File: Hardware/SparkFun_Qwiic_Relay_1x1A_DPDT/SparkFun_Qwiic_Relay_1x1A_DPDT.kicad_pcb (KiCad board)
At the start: 2 copper layers, 25.4 x 33.3 mm, 72 parts, among them J1 Qwiic_RA, J2 Conn_01x03, J3 Qwiic_RA, J4 Conn_01x01, J5 I2C, J6 3.5mm, K2 G6K-2F-Y DC3, Q2 LMUN2235LT1G, U1 PCA9536DP, U3 EL3H7

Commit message: Post review update
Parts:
- removed U1: PCA9536DP, SparkFun-Semiconductor-Standard:TSSOP-8_3x3mm_P0.65mm
- added JP1: ADR, SparkFun-Jumper:Jumper_2_NO, B.Cu at (151.8, 110.5)
- added R3: 10k, SparkFun-Resistor:R_0603_1608Metric, F.Cu at (153.4, 109.2)
- added U2: TCA9555RTWR, SparkFun-Semiconductor-Standard:QFN-24-1EP_4x4mm_P0.5mm_EP2.45x2.45mm, F.Cu at (148.0, 109.2)
- added kibuzzard-695DDFCB: G***, kibuzzard-695DDFCB, B.Cu at (154.8, 110.5)
- JP4: value ~ -> LED
- moved Ref** 14.9 mm to (140.3, 112.4)
- moved R2 7.94 mm to (144.1, 109.2), turned to -90 degrees
- moved C1 7.63 mm to (151.8, 109.2), turned to -90 degrees
- moved TP1 3.18 mm to (143.8, 107.6)
- moved TP2 1.27 mm to (143.8, 109.9)
- moved kibuzzard-693716F7 0.95 mm to (148.0, 107.3)
- moved D1 0.95 mm to (157.8, 109.2)
- moved D3 0.95 mm to (138.4, 109.2)
- moved D6 0.95 mm to (149.9, 102.2)
- moved D7 0.95 mm to (141.3, 97.8)
- moved FID4 0.95 mm to (159.7, 92.1)
- moved G*** 0.95 mm to (157.2, 99.1)
- moved G*** 0.95 mm to (139.1, 84.8)
- moved G*** 0.95 mm to (148.0, 103.8)
- moved J1 0.95 mm to (155.9, 103.8)
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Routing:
- net Net-(JP1-A): track 0.00 -> 8.66 mm, vias 0 -> 1
- net GND: track 13.0 -> 20.4 mm, vias 9 -> 12
- net STAT_LED: track 10.9 -> 6.48 mm, vias 2 -> 0
- net Ext_Drive: track 18.9 -> 23.2 mm, vias 1 -> 2
- net SCL: track 49.6 -> 46.5 mm
- net SDA: track 48.6 -> 45.5 mm
- net IO2: track 7.89 -> 5.35 mm
- net 3.3V: track 80.3 -> 82.6 mm, vias 6 -> 8
- net Net-(JP4-A): track 4.57 -> 3.92 mm
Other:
- board size 25.4 x 33.3 mm -> 25.4 x 34.3 mm

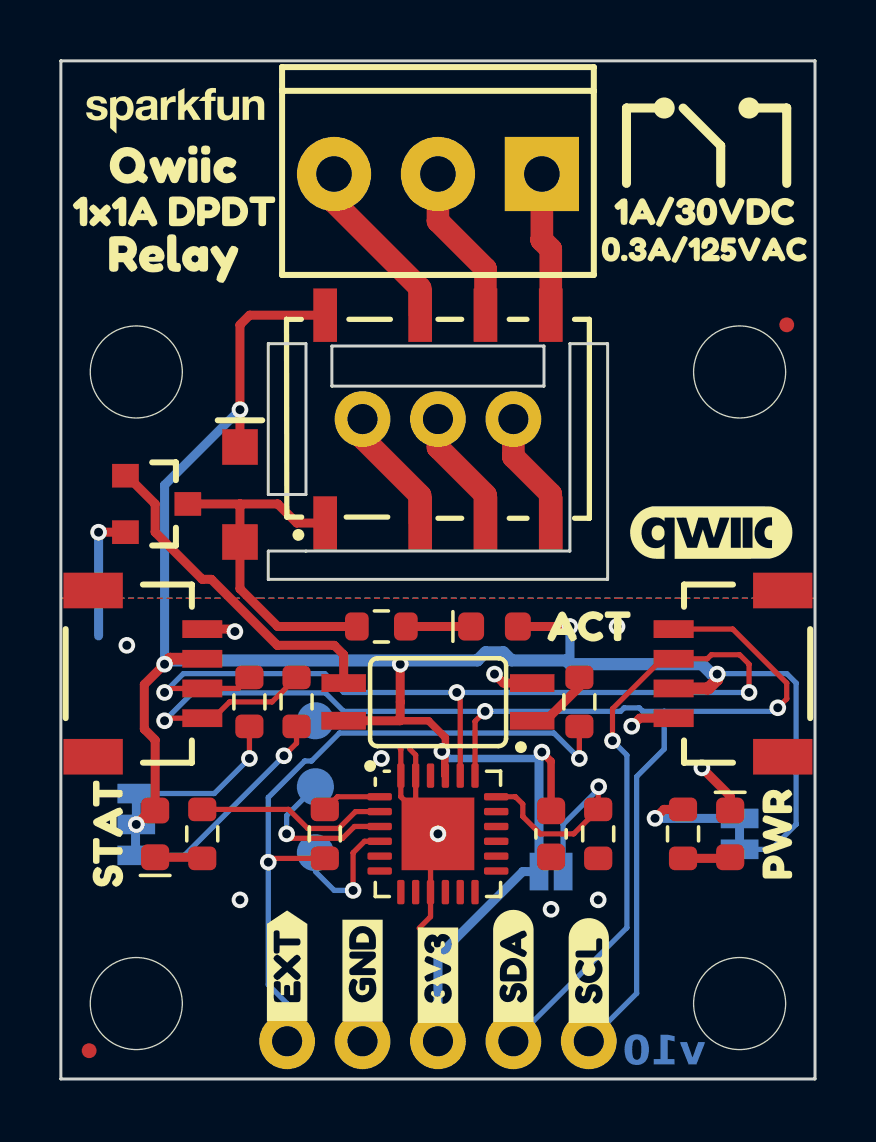
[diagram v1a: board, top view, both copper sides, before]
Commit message: Fix polarized relay. Increase version on PCB and SCH.
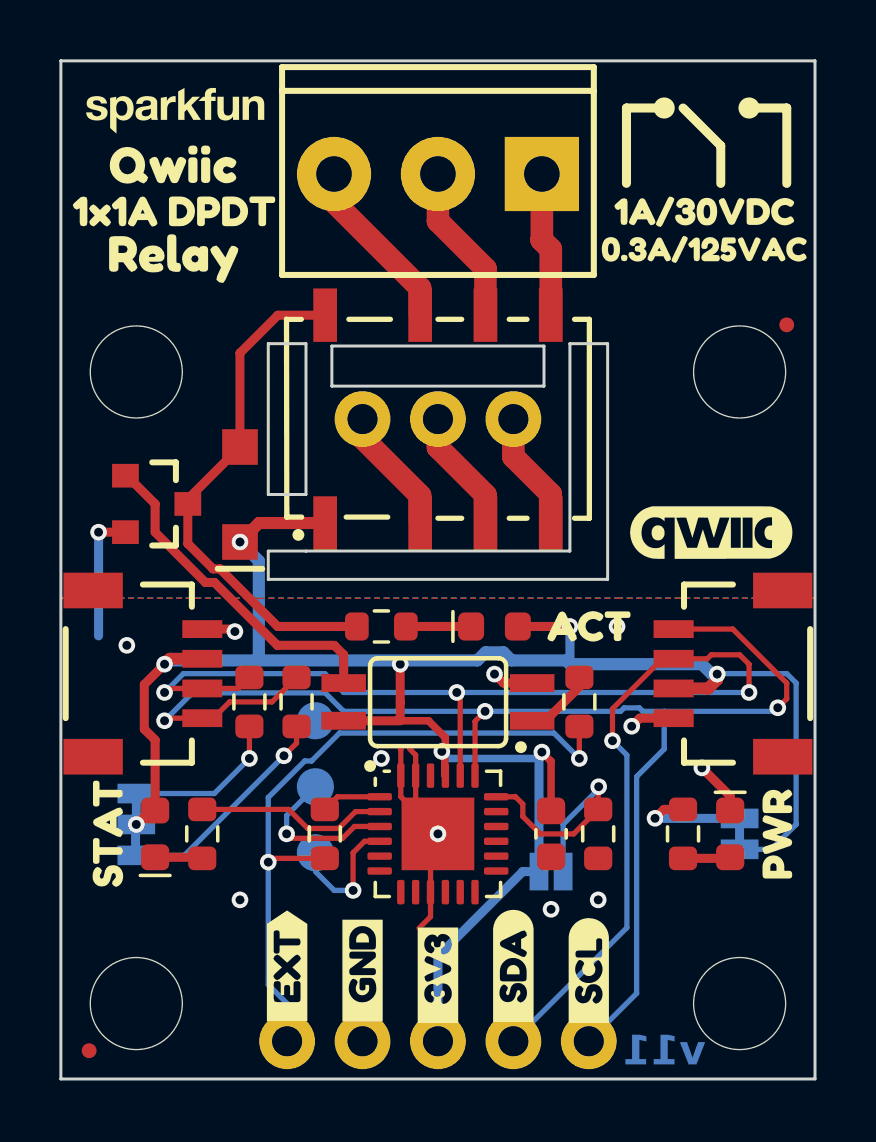
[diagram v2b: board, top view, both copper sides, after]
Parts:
- turned D7 to 90 degrees
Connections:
- K2 pad 1: Net-(D7-A) -> 3.3V
- K2 pad 8: 3.3V -> Net-(D7-A)
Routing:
- net 3.3V: track 82.6 -> 73.3 mm
- net Net-(D7-A): track 12.2 -> 17.4 mm
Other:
- board text added: "v11"
- board text removed: "v10"
